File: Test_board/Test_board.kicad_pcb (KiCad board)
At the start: 4 copper layers, 94 x 94 mm, 6 parts, among them J1 CONN_02X26, J2 CONN_02X26

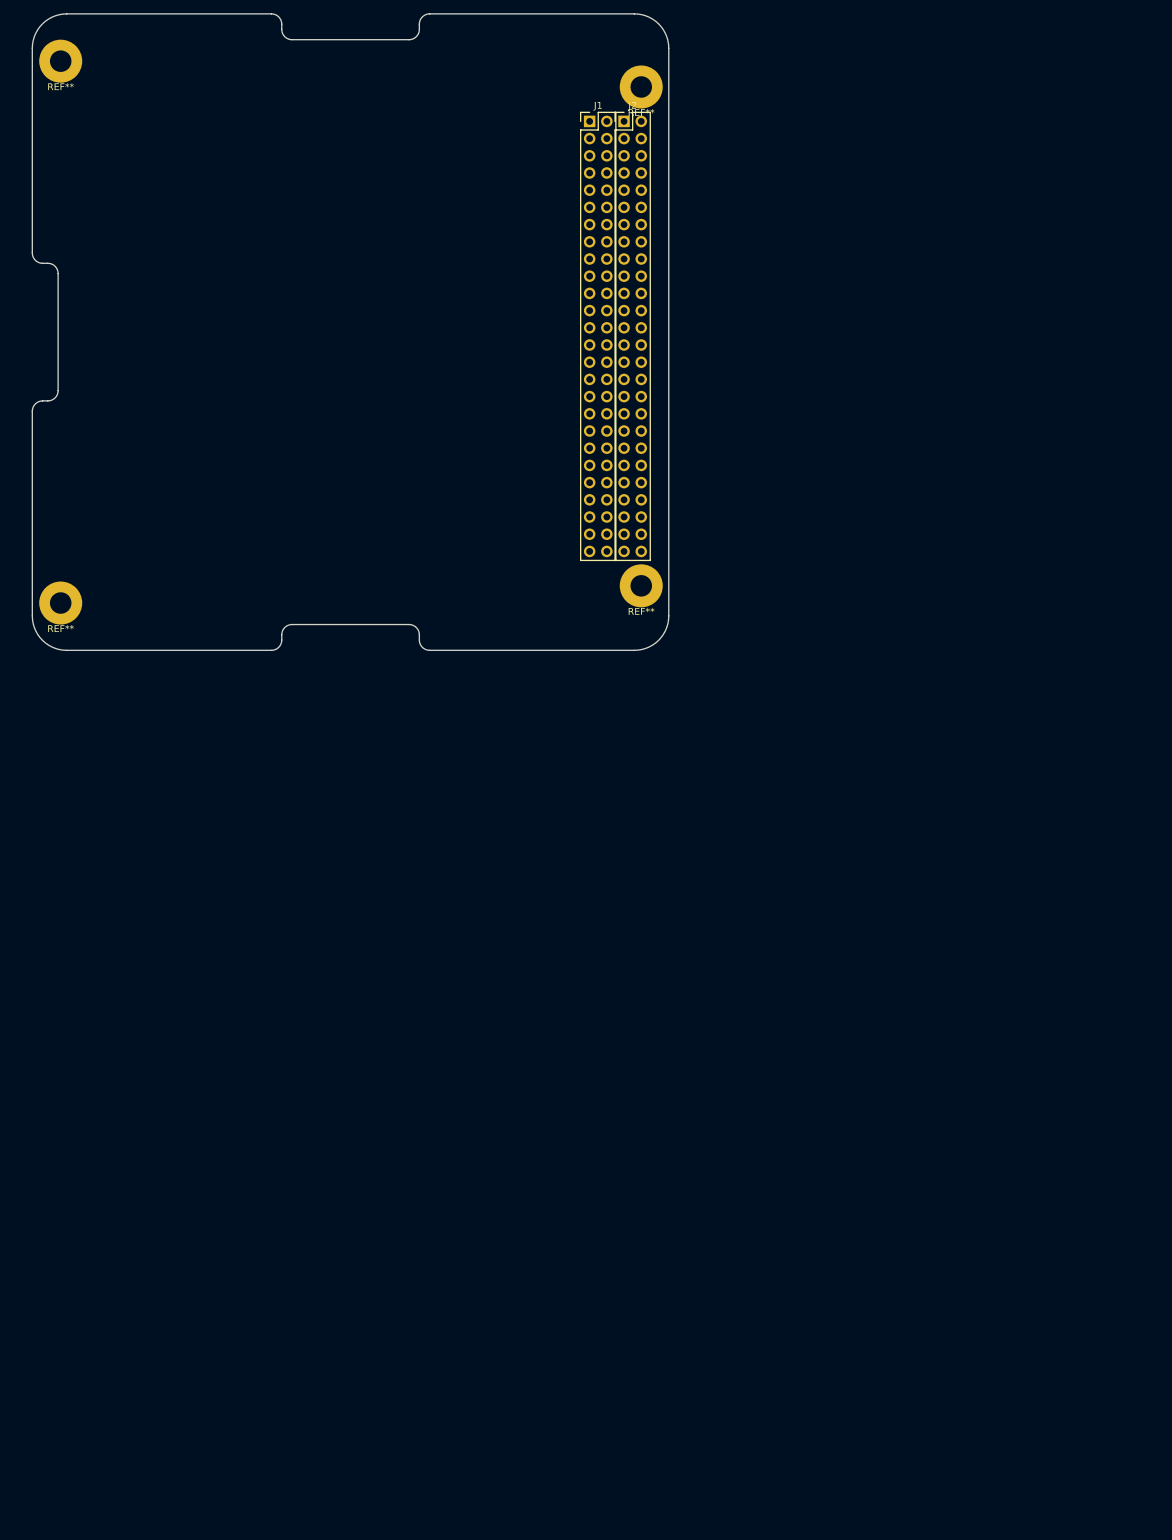
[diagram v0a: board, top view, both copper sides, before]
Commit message: Removed db9, created last footprints, finished assigning footprints, started pcb
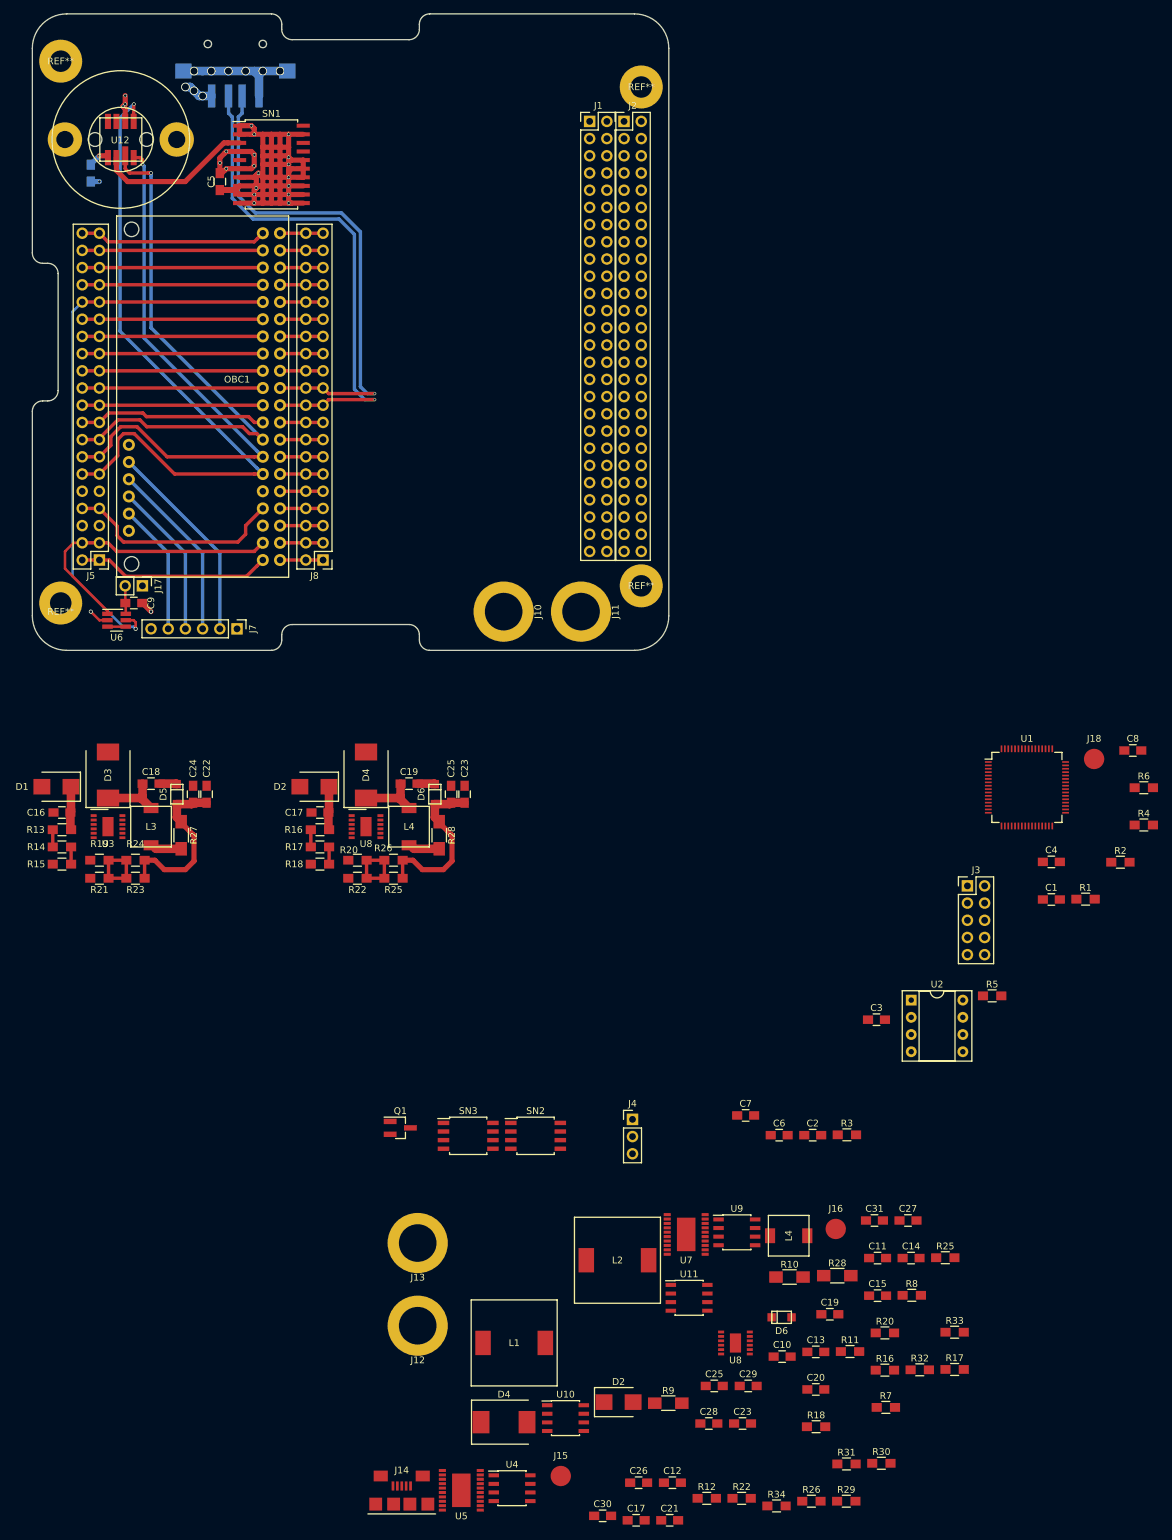
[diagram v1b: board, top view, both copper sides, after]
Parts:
- added C1: 0.1uF, Capacitors_SMD:C_0805_HandSoldering, F.Cu at (280.1, 158.3)
- added C10: 100uF, Capacitors_SMD:C_0805_HandSoldering, F.Cu at (240.4, 225.8)
- added C11: 47uF, Capacitors_SMD:C_0805_HandSoldering, F.Cu at (254.5, 211.3)
- added C12: 100uF, Capacitors_SMD:C_0805_HandSoldering, F.Cu at (224.2, 244.4)
- added C13: 47uF, Capacitors_SMD:C_0805_HandSoldering, F.Cu at (245.3, 225.1)
- added C14: 0.1uF, Capacitors_SMD:C_0805_HandSoldering, F.Cu at (259.4, 211.3)
- added C15: 0.1uF, Capacitors_SMD:C_0805_HandSoldering, F.Cu at (254.5, 216.8)
- added C16: 0.1uF, Capacitors_SMD:C_0805_HandSoldering, F.Cu at (134.0, 145.5)
- added C17: 0.1uF, Capacitors_SMD:C_0805_HandSoldering, F.Cu at (172.1, 145.5)
- added C17: 0.1uF, Capacitors_SMD:C_0805_HandSoldering, F.Cu at (218.8, 250.0)
- added C18: 1uF, Capacitors_SMD:C_0805_HandSoldering, F.Cu at (147.2, 141.2)
- added C19: 1uF, Capacitors_SMD:C_0805_HandSoldering, F.Cu at (185.3, 141.2)
- added C19: 1uF, Capacitors_SMD:C_0805_HandSoldering, F.Cu at (247.4, 219.6)
- added C2: 0.1uF, Capacitors_SMD:C_0805_HandSoldering, F.Cu at (244.9, 193.1)
- added C20: 0.1uF, Capacitors_SMD:C_0805_HandSoldering, F.Cu at (245.3, 230.7)
- added C21: 0.1uF, Capacitors_SMD:C_0805_HandSoldering, F.Cu at (223.8, 250.0)
- added C22: 10uF, Capacitors_SMD:C_0805_HandSoldering, F.Cu at (155.4, 142.8)
- added C23: 10uF, Capacitors_SMD:C_0805_HandSoldering, F.Cu at (193.5, 142.8)
- added C23: 10uF, Capacitors_SMD:C_0805_HandSoldering, F.Cu at (234.5, 235.7)
- added C24: 100uF, Capacitors_SMD:C_0805_HandSoldering, F.Cu at (153.4, 142.8)
- added C25: 100uF, Capacitors_SMD:C_0805_HandSoldering, F.Cu at (191.5, 142.8)
- added C25: 100uF, Capacitors_SMD:C_0805_HandSoldering, F.Cu at (230.4, 230.1)
- added C26: 12pF, Capacitors_SMD:C_0805_HandSoldering, F.Cu at (219.2, 244.4)
- added C27: 12pF, Capacitors_SMD:C_0805_HandSoldering, F.Cu at (259.0, 205.7)
- added C28: 680pF, Capacitors_SMD:C_0805_HandSoldering, F.Cu at (229.6, 235.7)
- added C29: 680pF, Capacitors_SMD:C_0805_HandSoldering, F.Cu at (235.4, 230.1)
- added C3: 0.1uF, Capacitors_SMD:C_0805_HandSoldering, F.Cu at (254.3, 176.1)
- added C30: 47pF, Capacitors_SMD:C_0805_HandSoldering, F.Cu at (213.9, 249.3)
- added C31: 47pF, Capacitors_SMD:C_0805_HandSoldering, F.Cu at (254.0, 205.7)
- added C32: 0.1uF, Capacitors_SMD:C_0805_HandSoldering, B.Cu at (138.3, 51.0)
- added C4: 0.1uF, Capacitors_SMD:C_0805_HandSoldering, F.Cu at (280.1, 152.8)
- added C5: 0.1uF, Capacitors_SMD:C_0805_HandSoldering, F.Cu at (157.3, 52.3)
- added C6: 0.1uF, Capacitors_SMD:C_0805_HandSoldering, F.Cu at (239.9, 193.1)
- added C7: 0.1uF, Capacitors_SMD:C_0805_HandSoldering, F.Cu at (235.0, 190.2)
- added C8: 0.1uF, Capacitors_SMD:C_0805_HandSoldering, F.Cu at (292.2, 136.3)
- added C9: 0.1uF, Capacitors_SMD:C_0805_HandSoldering, F.Cu at (144.6, 114.5)
- added D1: MBRS140, Diodes_SMD:D_SMB, F.Cu at (133.2, 141.7)
- added D2: MBRS140, Diodes_SMD:D_SMB, F.Cu at (171.3, 141.7)
- added D2: MBRS140, Diodes_SMD:D_SMB, F.Cu at (216.2, 232.5)
- added D3: MBRS340, Diodes_SMD:D_SMC, F.Cu at (140.8, 139.9)
- added D4: MBRS340, Diodes_SMD:D_SMC, F.Cu at (178.9, 139.9)
- added D4: MBRS340, Diodes_SMD:D_SMC, F.Cu at (199.3, 235.5)
- added D5: D, aleksandr_footprints:SOD-123FL, F.Cu at (151.0, 142.7)
- added D6: D, aleksandr_footprints:SOD-123FL, F.Cu at (189.1, 142.7)
- added D6: D, aleksandr_footprints:SOD-123FL, F.Cu at (240.3, 220.0)
- added J10: 4.19mmBananaJack, aleksandr_footprints:4.19Banana, F.Cu at (199.3, 115.8)
- added J11: 4.19mmBananaJack, aleksandr_footprints:4.19Banana, F.Cu at (210.7, 115.8)
- added J12: 4.19mmBananaJack, aleksandr_footprints:4.19Banana, F.Cu at (186.6, 221.2)
- added J13: 4.19mmBananaJack, aleksandr_footprints:4.19Banana, F.Cu at (186.6, 209.0)
- added J14: USB_OTG, aleksandr_footprints:micro_usb_smd, F.Cu at (184.2, 247.6)
- added J15: TEST_1P, Measurement_Points:Measurement_Point_Round-SMD-Pad_Big, F.Cu at (207.7, 243.4)
- added J16: TEST_1P, Measurement_Points:Measurement_Point_Round-SMD-Pad_Big, F.Cu at (248.3, 207.0)
- added J17: Conn_01x02, Pin_Headers:Pin_Header_Straight_1x02_Pitch2.54mm, F.Cu at (145.9, 112.0)
- added J18: TEST_1P, Measurement_Points:Measurement_Point_Round-SMD-Pad_Big, F.Cu at (286.4, 137.6)
- added J3: Conn_02x05_Odd_Even, Pin_Headers:Pin_Header_Straight_2x05_Pitch2.54mm, F.Cu at (267.7, 156.3)
- added J4: Conn_01x03, Pin_Headers:Pin_Header_Straight_1x03_Pitch2.54mm, F.Cu at (218.3, 190.8)
- added J5: Conn_02x20_Odd_Even, Pin_Headers:Pin_Header_Straight_2x20_Pitch2.54mm, F.Cu at (139.6, 108.2)
- added J7: Conn_01x06, Pin_Headers:Pin_Header_Straight_1x06_Pitch2.54mm, F.Cu at (159.9, 118.3)
- added J8: Conn_02x20_Odd_Even, Pin_Headers:Pin_Header_Straight_2x20_Pitch2.54mm, F.Cu at (172.6, 108.2)
- added J9: USB_A, aleksandr_footprints:USB_A_Board, B.Cu at (159.6, 32.0)
- added L1: 2.2uH, aleksandr_footprints:L-7443330220, F.Cu at (200.8, 223.8)
- added L2: 2.2uH, aleksandr_footprints:L-7443330220, F.Cu at (216.1, 211.6)
- added L3: 6.8uH, aleksandr_footprints:L-SLF6028T-6R8M1R5-PF, F.Cu at (147.2, 147.5)
- added L4: 6.8uH, aleksandr_footprints:L-SLF6028T-6R8M1R5-PF, F.Cu at (185.3, 147.5)
- added L4: 6.8uH, aleksandr_footprints:L-SLF6028T-6R8M1R5-PF, F.Cu at (241.3, 208.0)
- added OBC1: Arietta_G25, aleksandr_footprints:Arietta_G25, F.Cu at (166.2, 59.9)
- added Q1: Q_NMOS_GSD, TO_SOT_Packages_SMD:SOT-23_Handsoldering, F.Cu at (184.0, 192.0)
- added R1: 4k7, Resistors_SMD:R_0805_HandSoldering, F.Cu at (285.2, 158.3)
- added R10: 20m, Resistors_SMD:R_1206_HandSoldering, F.Cu at (241.5, 214.1)
- added R11: 825k, Resistors_SMD:R_0805_HandSoldering, F.Cu at (250.4, 225.1)
- added R12: 182k, Resistors_SMD:R_0805_HandSoldering, F.Cu at (229.2, 246.7)
- added R13: 100k, Resistors_SMD:R_0805_HandSoldering, F.Cu at (134.0, 148.0)
- added R14: 100k, Resistors_SMD:R_0805_HandSoldering, F.Cu at (134.0, 150.5)
- added R15: 100k, Resistors_SMD:R_0805_HandSoldering, F.Cu at (134.0, 153.1)
- added R16: 100k, Resistors_SMD:R_0805_HandSoldering, F.Cu at (172.1, 148.0)
- added R16: 100k, Resistors_SMD:R_0805_HandSoldering, F.Cu at (255.5, 227.8)
- added R17: 100k, Resistors_SMD:R_0805_HandSoldering, F.Cu at (172.1, 150.5)
- added R17: 100k, Resistors_SMD:R_0805_HandSoldering, F.Cu at (265.8, 227.7)
- added R18: 100k, Resistors_SMD:R_0805_HandSoldering, F.Cu at (172.1, 153.1)
- added R18: 100k, Resistors_SMD:R_0805_HandSoldering, F.Cu at (245.4, 236.2)
- added R19: 179k, Resistors_SMD:R_0805_HandSoldering, F.Cu at (139.6, 152.5)
- added R2: 4k7, Resistors_SMD:R_0805_HandSoldering, F.Cu at (290.3, 152.8)
- added R20: 179k, Resistors_SMD:R_0805_HandSoldering, F.Cu at (177.7, 152.5)
- added R20: 179k, Resistors_SMD:R_0805_HandSoldering, F.Cu at (255.5, 222.3)
- added R21: 330k, Resistors_SMD:R_0805_HandSoldering, F.Cu at (139.6, 155.2)
- added R22: 330k, Resistors_SMD:R_0805_HandSoldering, F.Cu at (177.7, 155.2)
- added R22: 330k, Resistors_SMD:R_0805_HandSoldering, F.Cu at (234.4, 246.7)
- added R23: 180k, Resistors_SMD:R_0805_HandSoldering, F.Cu at (144.9, 155.2)
- added R24: 180k, Resistors_SMD:R_0805_HandSoldering, F.Cu at (144.9, 152.5)
- added R25: 180k, Resistors_SMD:R_0805_HandSoldering, F.Cu at (183.0, 155.2)
- added R25: 180k, Resistors_SMD:R_0805_HandSoldering, F.Cu at (264.5, 211.2)
- added R26: 180k, Resistors_SMD:R_0805_HandSoldering, F.Cu at (183.0, 152.5)
- added R26: 180k, Resistors_SMD:R_0805_HandSoldering, F.Cu at (244.7, 247.2)
- added R27: 50m, Resistors_SMD:R_1206_HandSoldering, F.Cu at (151.6, 148.8)
- added R28: 50m, Resistors_SMD:R_1206_HandSoldering, F.Cu at (189.7, 148.8)
- added R28: 50m, Resistors_SMD:R_1206_HandSoldering, F.Cu at (248.5, 213.9)
- added R29: 49.9k, Resistors_SMD:R_0805_HandSoldering, F.Cu at (249.8, 247.2)
- added R3: 4k7, Resistors_SMD:R_0805_HandSoldering, F.Cu at (249.9, 193.1)
- added R30: 49.9k, Resistors_SMD:R_0805_HandSoldering, F.Cu at (255.0, 241.6)
- added R31: 887k, Resistors_SMD:R_0805_HandSoldering, F.Cu at (249.9, 241.7)
- added R32: 121k, Resistors_SMD:R_0805_HandSoldering, F.Cu at (260.7, 227.8)
- added R33: 6.49k, Resistors_SMD:R_0805_HandSoldering, F.Cu at (265.8, 222.2)
- added R34: 6.49k, Resistors_SMD:R_0805_HandSoldering, F.Cu at (239.5, 247.9)
- added R4: 4K7, Resistors_SMD:R_0805_HandSoldering, F.Cu at (293.8, 147.3)
- added R5: 1k, Resistors_SMD:R_0805_HandSoldering, F.Cu at (271.4, 172.5)
- added R6: 1k, Resistors_SMD:R_0805_HandSoldering, F.Cu at (293.8, 141.8)
- added R7: 90.9k, Resistors_SMD:R_0805_HandSoldering, F.Cu at (255.7, 233.3)
- added R8: 90.9k, Resistors_SMD:R_0805_HandSoldering, F.Cu at (259.5, 216.8)
- added R9: 20m, Resistors_SMD:R_1206_HandSoldering, F.Cu at (223.6, 232.7)
- added SN1: DS3232, Housings_SOIC:SOIC-20W_7.5x12.8mm_Pitch1.27mm, F.Cu at (165.0, 49.8)
- added SN2: DS1624, Housings_SOIC:SOIJ-8_5.3x5.3mm_Pitch1.27mm, F.Cu at (204.0, 193.2)
- added SN3: DS1624, Housings_SOIC:SOIJ-8_5.3x5.3mm_Pitch1.27mm, F.Cu at (194.0, 193.2)
- added U1: STM32F303RE, Housings_QFP:LQFP-64_10x10mm_Pitch0.5mm, F.Cu at (276.5, 141.8)
- added U10: INA219, Housings_SOIC:SOIC-8_3.9x4.9mm_Pitch1.27mm, F.Cu at (208.4, 234.9)
- added U11: INA219, Housings_SOIC:SOIC-8_3.9x4.9mm_Pitch1.27mm, F.Cu at (226.6, 217.1)
- added U12: MS5540C, aleksandr_footprints:MS5540C, F.Cu at (142.7, 46.1)
- added U2: 24LC256, Housings_DIP:DIP-8_W7.62mm_Socket, F.Cu at (259.4, 173.2)
- added U3: LT3652, aleksandr_footprints:12MSOP-E, F.Cu at (140.8, 147.5)
- added U4: INA219, Housings_SOIC:SOIC-8_3.9x4.9mm_Pitch1.27mm, F.Cu at (200.5, 245.2)
- added U5: LTC3113, aleksandr_footprints:20TSSOP-E, F.Cu at (193.0, 245.5)
- added U6: MAX6730A, TO_SOT_Packages_SMD:SOT-23-6_Handsoldering, F.Cu at (142.1, 117.1)
- added U7: LTC3113, aleksandr_footprints:20TSSOP-E, F.Cu at (226.2, 207.8)
- added U8: LT3652, aleksandr_footprints:12MSOP-E, F.Cu at (178.9, 147.5)
- added U8: LT3652, aleksandr_footprints:12MSOP-E, F.Cu at (233.5, 223.8)
- added U9: INA219, Housings_SOIC:SOIC-8_3.9x4.9mm_Pitch1.27mm, F.Cu at (233.7, 207.5)
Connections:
- J1 pad 1: Net-(J1-Pad1) -> +3V3
- J1 pad 13: Net-(J1-Pad13) -> /SDA0
- J1 pad 14: Net-(J1-Pad14) -> /SDA0
- J1 pad 15: Net-(J1-Pad15) -> /SCL0
- J1 pad 16: Net-(J1-Pad16) -> /SCL0
- J1 pad 17: Net-(J1-Pad17) -> /ARM_SPI1_SCK
- J1 pad 18: Net-(J1-Pad18) -> GND
- J1 pad 19: Net-(J1-Pad19) -> /ARM_SPI1_MISO
- J1 pad 2: Net-(J1-Pad2) -> +3V3
- J1 pad 20: Net-(J1-Pad20) -> GND
- J1 pad 21: Net-(J1-Pad21) -> /ARM_SPI1_MOSI
- J1 pad 22: Net-(J1-Pad22) -> GND
- J1 pad 23: Net-(J1-Pad23) -> /ARM_UART2_MISO
- J1 pad 24: Net-(J1-Pad24) -> GND
- J1 pad 25: Net-(J1-Pad25) -> /ARM_UART2_MOSI
- J1 pad 26: Net-(J1-Pad26) -> GND
- J1 pad 27: Net-(J1-Pad27) -> /ARM_USB_D-
- J1 pad 28: Net-(J1-Pad28) -> GND
- J1 pad 29: Net-(J1-Pad29) -> /ARM_USB_D+
- J1 pad 3: Net-(J1-Pad3) -> +3V3
- J1 pad 30: Net-(J1-Pad30) -> GND
- J1 pad 31: Net-(J1-Pad31) -> GND
- J1 pad 32: Net-(J1-Pad32) -> GND
- J1 pad 33: Net-(J1-Pad33) -> /CAN_RX
- J1 pad 34: Net-(J1-Pad34) -> GND
- J1 pad 35: Net-(J1-Pad35) -> /CAN_TX
- J1 pad 36: Net-(J1-Pad36) -> GND
- J1 pad 37: Net-(J1-Pad37) -> GND
- J1 pad 38: Net-(J1-Pad38) -> GND
- J1 pad 4: Net-(J1-Pad4) -> +3V3
- J1 pad 45: Net-(J1-Pad45) -> +BATT
- J1 pad 46: Net-(J1-Pad46) -> +BATT
- J1 pad 47: Net-(J1-Pad47) -> +BATT
- J1 pad 48: Net-(J1-Pad48) -> +BATT
- J1 pad 49: Net-(J1-Pad49) -> +BATT
- J1 pad 5: Net-(J1-Pad5) -> +3V3
- J1 pad 50: Net-(J1-Pad50) -> +BATT
- J1 pad 51: Net-(J1-Pad51) -> +BATT
- J1 pad 52: Net-(J1-Pad52) -> +BATT
- J1 pad 6: Net-(J1-Pad6) -> +3V3
- J1 pad 7: Net-(J1-Pad7) -> +3V3
- J1 pad 8: Net-(J1-Pad8) -> +3V3
- J2 pad 1: Net-(J2-Pad1) -> GND
- J2 pad 13: Net-(J2-Pad13) -> /SDA0
- J2 pad 14: Net-(J2-Pad14) -> /SDA0
- J2 pad 15: Net-(J2-Pad15) -> /SCL0
- J2 pad 16: Net-(J2-Pad16) -> /SCL0
- J2 pad 2: Net-(J2-Pad2) -> GND
- J2 pad 3: Net-(J2-Pad3) -> GND
- J2 pad 4: Net-(J2-Pad4) -> GND
- J2 pad 45: Net-(J2-Pad45) -> GND
- J2 pad 46: Net-(J2-Pad46) -> GND
- J2 pad 47: Net-(J2-Pad47) -> GND
- J2 pad 48: Net-(J2-Pad48) -> GND
- J2 pad 49: Net-(J2-Pad49) -> GND
- J2 pad 5: Net-(J2-Pad5) -> GND
- J2 pad 50: Net-(J2-Pad50) -> GND
- J2 pad 51: Net-(J2-Pad51) -> GND
- J2 pad 52: Net-(J2-Pad52) -> GND
- J2 pad 6: Net-(J2-Pad6) -> GND
- J2 pad 7: Net-(J2-Pad7) -> GND
- J2 pad 8: Net-(J2-Pad8) -> GND
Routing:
- net GND: track 0.00 -> 152.0 mm, vias 0 -> 24
- net /BARO_CLK: track 0.00 -> 99.8 mm, vias 0 -> 1
- net /BARO_MISO: track 0.00 -> 83.7 mm, vias 0 -> 1
- net /WDT_KICK: track 0.00 -> 82.8 mm, vias 0 -> 1
- net /BARO_MOSI: track 0.00 -> 81.4 mm, vias 0 -> 1
- net /USB_D-: track 0.00 -> 77.5 mm, vias 0 -> 1
- net /USB_D+: track 0.00 -> 76.0 mm, vias 0 -> 1
- net /POWER/MPPT_OUT: track 0.00 -> 50.1 mm
- net /~OBC_RST: track 0.00 -> 42.6 mm
- net Net-(J5-Pad7): track 0.00 -> 32.3 mm
- net Net-(J7-Pad2): track 0.00 -> 30.2 mm
- net Net-(J5-Pad1): track 0.00 -> 28.7 mm
- net Net-(J5-Pad17): track 0.00 -> 27.8 mm
- net /EEPROM_WP: track 0.00 -> 27.7 mm
- net Net-(J5-Pad37): track 0.00 -> 26.7 mm
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- added copper zone on PWR, net +3V3
- added copper zone on GND, net GND
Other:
- net class 10mil added: clearance 0.254, trace_width 0.254, via_dia 0.6, via_drill 0.4
- net class 15mil added: clearance 0.254, trace_width 0.381, via_dia 0.6, via_drill 0.4
- net class Default: clearance 0.2 -> 0.381; trace_width 0.25 -> 0.508
- rule trace_clearance: 0.2 -> 0.381
- rule trace_min: 0.2 -> 0.0762
- rule via_min_drill: 0.3 -> 0.254
- rule via_min_size: 0.4 -> 0.381
